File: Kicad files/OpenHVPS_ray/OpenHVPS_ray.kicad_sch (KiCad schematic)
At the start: 69 parts, among them J1 Conn_01x03_Male, J2 Conn_01x03_Male, Q1 FQT7N10, Q2 BC846A, Q3 MMDT3906, U1 MAX6008AEUR+T, U2 74HC14, U3 MAX4162, U4 CD14538BM

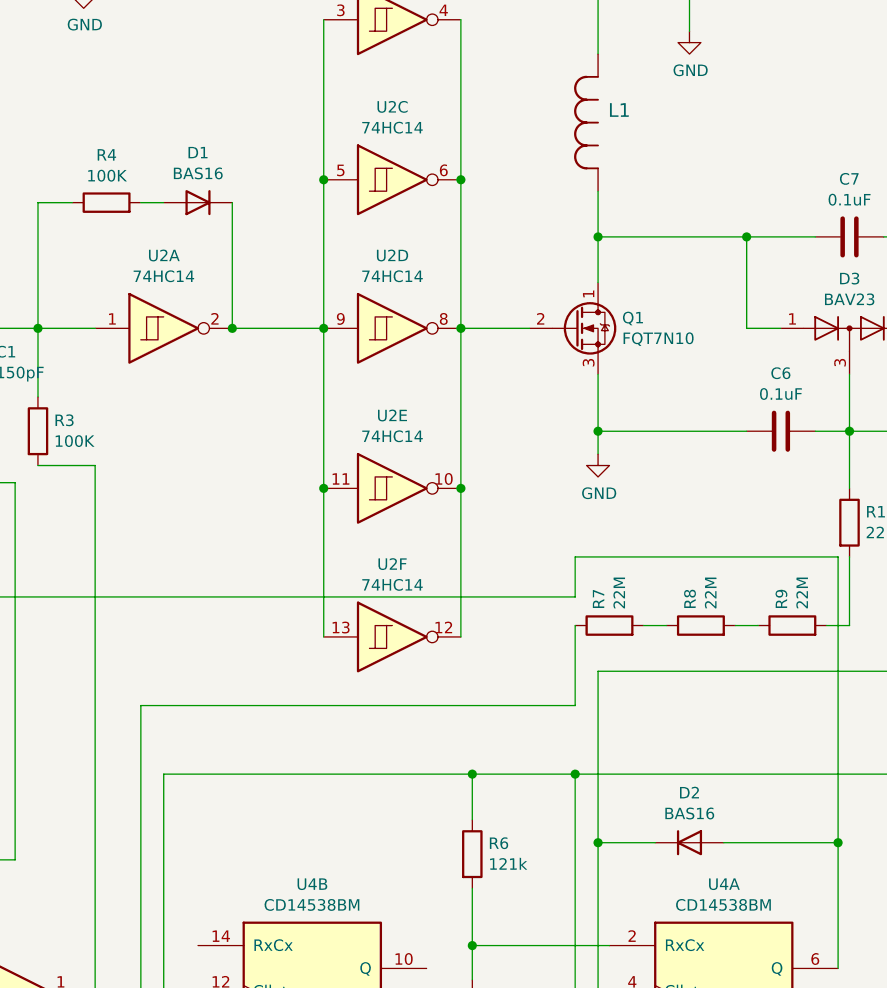
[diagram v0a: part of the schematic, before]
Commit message: fixed a couple of errors in BOM. reduced size of 2 diodes
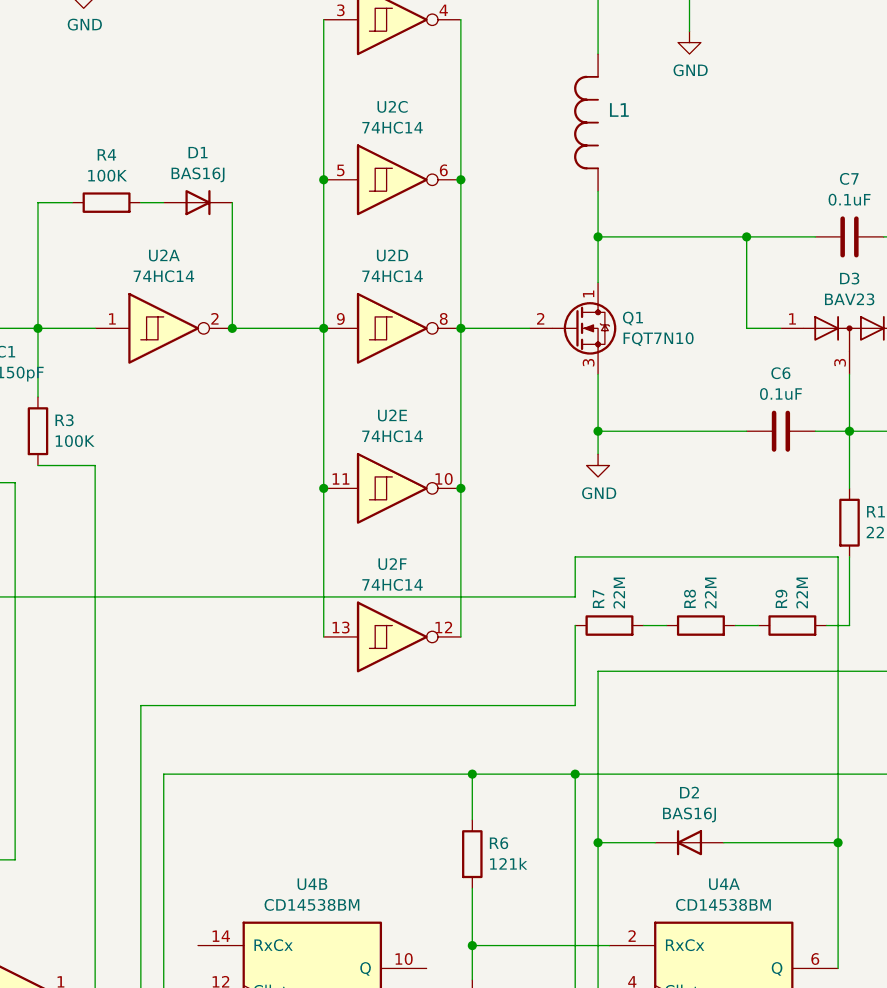
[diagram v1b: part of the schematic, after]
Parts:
- D1, D2: value BAS16 -> BAS16J; footprint Diode_SMD:D_SOT-23_ANK -> Diode_SMD:D_SOD-323F
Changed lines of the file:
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@@
     (in_bom yes) (on_board yes)
     (property "Reference" "D1" (id 0) (at 71.12 68.7832 0))
-    (property "Value" "BAS16" (id 1) (at 71.12 71.095 0))
-    (property "Footprint" "Diode_SMD:D_SOT-23_ANK" (id 2) (at 71.12 69.85 0)
-      (effects (font (size 1.27 1.27)) hide)
-    )
-    (property "Datasheet" "https://www.vishay.com/docs/85748/1n4148w.pdf" (id 3) (at 71.12 74.295 0)
+    (property "Value" "BAS16J" (id 1) (at 71.12 71.095 0))
+    (property "Footprint" "Diode_SMD:D_SOD-323F" (id 2) (at 71.12 69.85 0)
+      (effects (font (size 1.27 1.27)) hide)
+    )
+    (property "Datasheet" "https://www.digikey.com/en/products/detail/nexperia-usa-inc/BAS16J135/2405996" (id 3) (at 71.12 74.295 0)
       (effects (font (size 1.27 1.27)) hide)
     )
@@
     (in_bom yes) (on_board yes)
     (property "Reference" "D2" (id 0) (at 125.73 139.9032 0))
-    (property "Value" "BAS16" (id 1) (at 125.73 142.2146 0))
-    (property "Footprint" "Diode_SMD:D_SOT-23_ANK" (id 2) (at 125.73 149.86 0)
-      (effects (font (size 1.27 1.27)) hide)
-    )
-    (property "Datasheet" "https://www.vishay.com/docs/85748/1n4148w.pdf" (id 3) (at 125.73 145.415 0)
+    (property "Value" "BAS16J" (id 1) (at 125.73 142.2146 0))
+    (property "Footprint" "Diode_SMD:D_SOD-323F" (id 2) (at 125.73 149.86 0)
+      (effects (font (size 1.27 1.27)) hide)
+    )
+    (property "Datasheet" "https://www.digikey.com/en/products/detail/nexperia-usa-inc/BAS16J135/2405996" (id 3) (at 125.73 145.415 0)
       (effects (font (size 1.27 1.27)) hide)
     )
@@
       (effects (font (size 1.27 1.27)) (justify left) hide)
     )
-    (property "Datasheet" "http://www.ti.com/lit/ds/symlink/tlv2375.pdf" (id 3) (at 49.53 156.845 0)
+    (property "Datasheet" "https://www.digikey.com/en/products/detail/maxim-integrated/MAX4162EUK-T/470825" (id 3) (at 49.53 156.845 0)
       (effects (font (size 1.27 1.27)) hide)
     )
@@
       (effects (font (size 1.27 1.27)) hide)
     )
-    (property "Datasheet" "https://assets.nexperia.com/documents/data-sheet/HEF4538B.pdf" (id 3) (at 156.21 163.195 0)
+    (property "Datasheet" "https://www.digikey.com/en/products/detail/texas-instruments/CD14538BM/1690553" (id 3) (at 156.21 163.195 0)
       (effects (font (size 1.27 1.27)) hide)
     )
@@
       (effects (font (size 1.27 1.27)) hide)
     )
-    (property "Datasheet" "https://assets.nexperia.com/documents/data-sheet/HEF4538B.pdf" (id 3) (at 83.82 161.925 0)
+    (property "Datasheet" "https://www.digikey.com/en/products/detail/texas-instruments/CD14538BM/1690553" (id 3) (at 83.82 161.925 0)
       (effects (font (size 1.27 1.27)) hide)
     )
@@
       (effects (font (size 1.27 1.27)) hide)
     )
-    (property "Datasheet" "https://assets.nexperia.com/documents/data-sheet/HEF4538B.pdf" (id 3) (at 129.54 161.925 0)
+    (property "Datasheet" "https://www.digikey.com/en/products/detail/texas-instruments/CD14538BM/1690553" (id 3) (at 129.54 161.925 0)
       (effects (font (size 1.27 1.27)) hide)
     )
@@
     )
     (path "/00000000-0000-0000-0000-0000600ddc6a"
-      (reference "D1") (unit 1) (value "BAS16") (footprint "Diode_SMD:D_SOT-23_ANK")
+      (reference "D1") (unit 1) (value "BAS16J") (footprint "Diode_SMD:D_SOD-323F")
     )
     (path "/00000000-0000-0000-0000-00006007dc1b"
-      (reference "D2") (unit 1) (value "BAS16") (footprint "Diode_SMD:D_SOT-23_ANK")
+      (reference "D2") (unit 1) (value "BAS16J") (footprint "Diode_SMD:D_SOD-323F")
     )
     (path "/00000000-0000-0000-0000-00005ff5fed2"

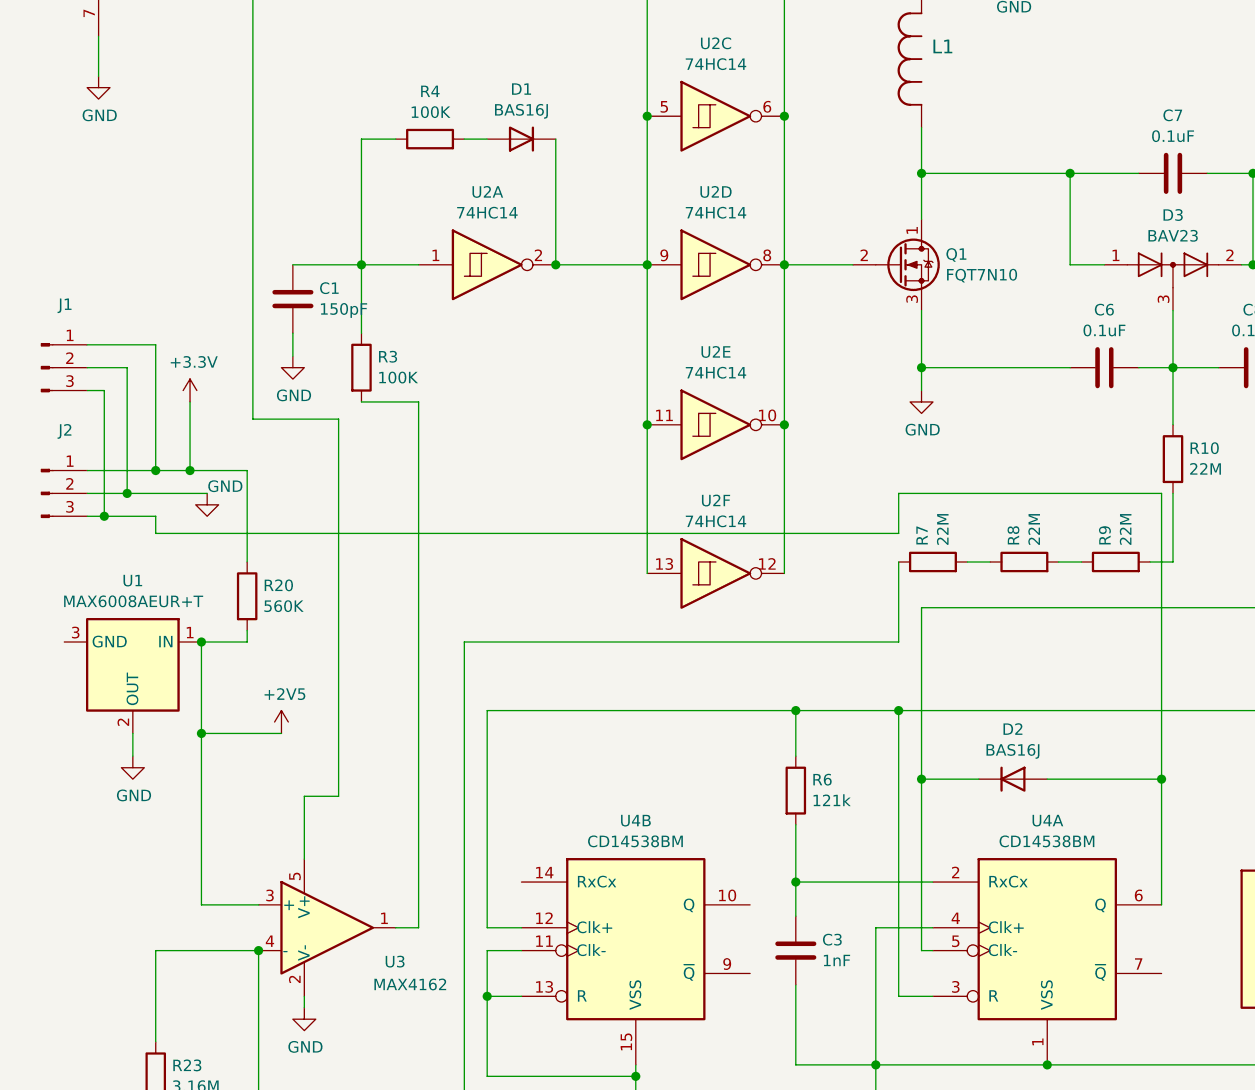
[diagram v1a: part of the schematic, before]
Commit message: Added a fuse for reverse polarity protection
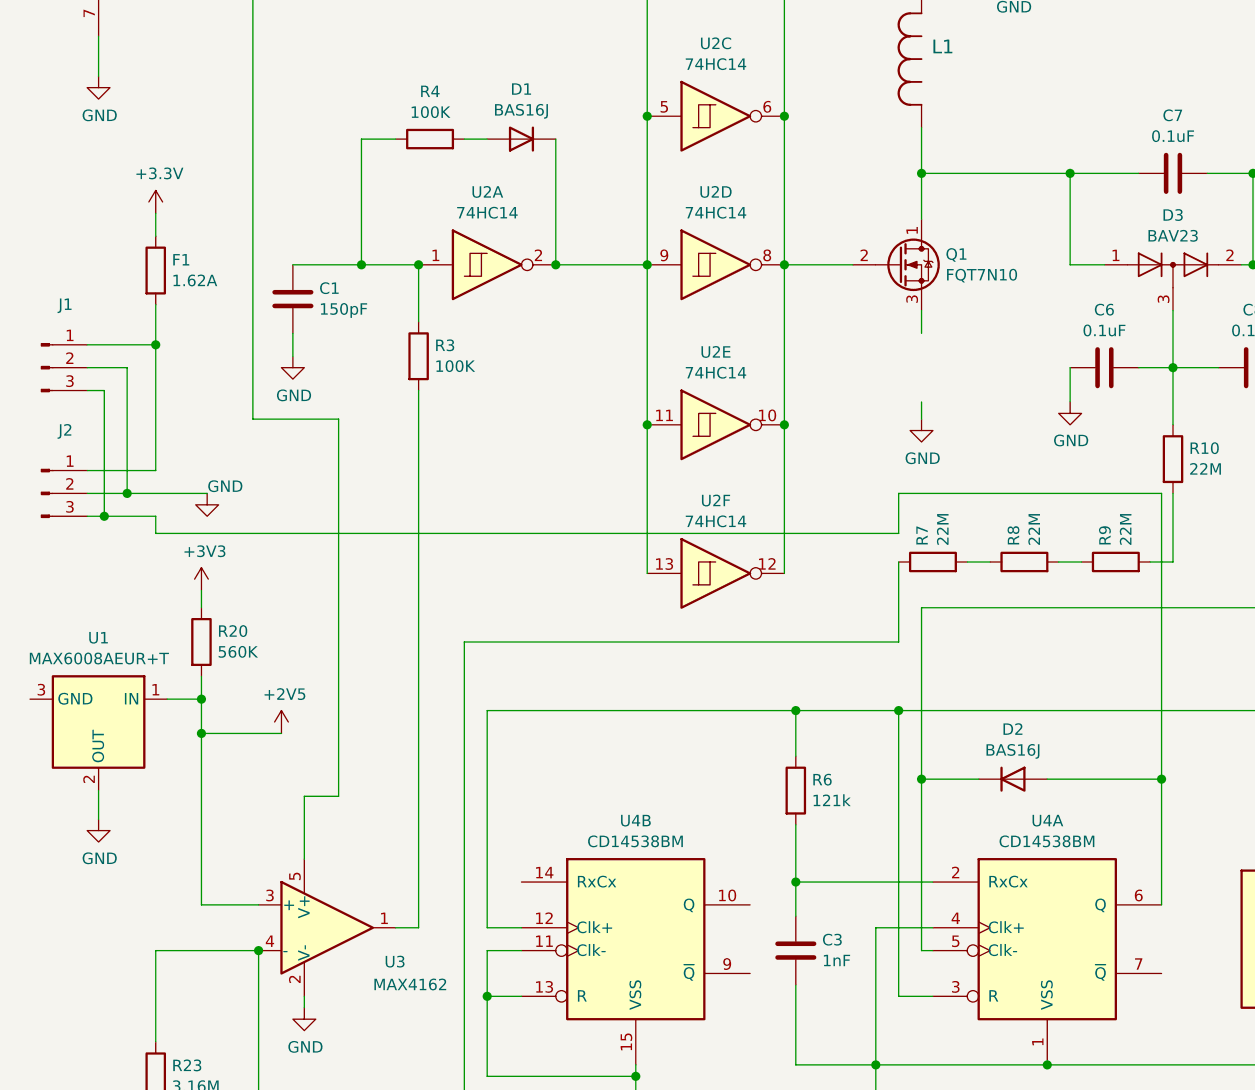
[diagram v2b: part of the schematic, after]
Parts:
- added F1: 1.62A, Resistor_SMD:R_0805_2012Metric, symbol Device:R
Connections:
- net +3V3: now also F1.1; no longer J1.1 (Pin_1), J2.1 (Pin_1)
- net GND: no longer Q1.3 (S)
- new net: F1.2, J1.1 (Pin_1), J2.1 (Pin_1)
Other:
- moved on the sheet: R20, R3, U1
